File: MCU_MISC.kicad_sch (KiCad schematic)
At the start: 61 parts, among them J4 Conn_ARM_JTAG_SWD_20, J5 Conn_01x03, J6 Conn_01x03, J7 SMA, J8 SMA, SW1 焊盘, SW2 Push_Button, SW3 Push_Button, SW4 Push_Button, U10 TJA1044GTK/3Z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

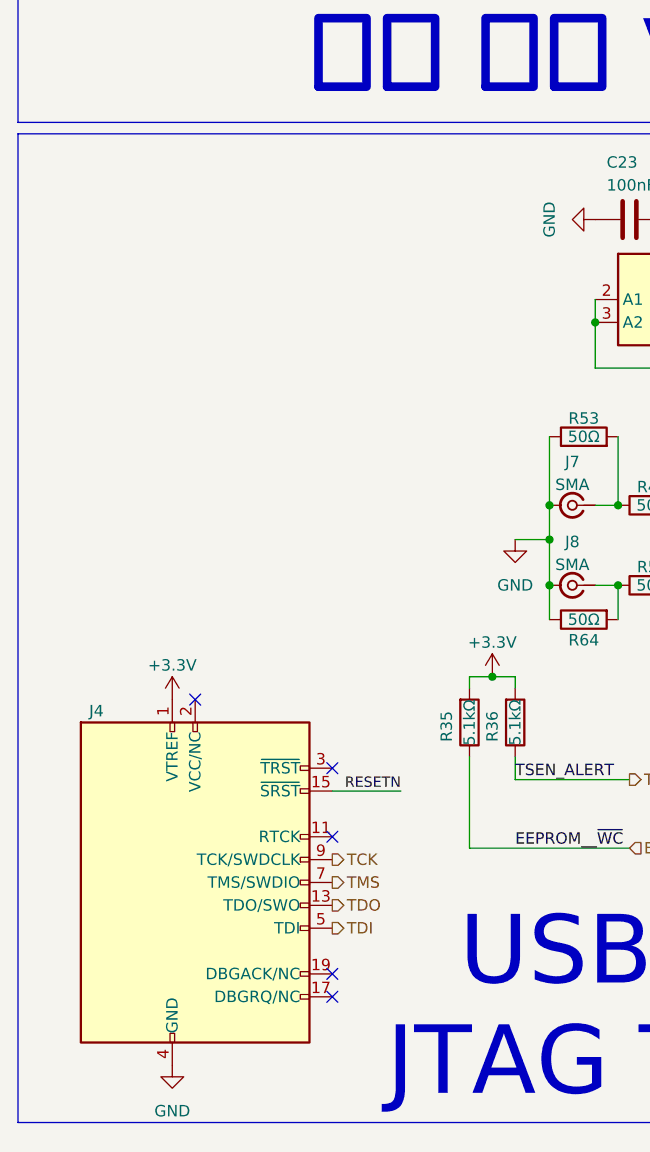
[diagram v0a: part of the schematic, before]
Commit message: 添加JTAG接口的ESD保护
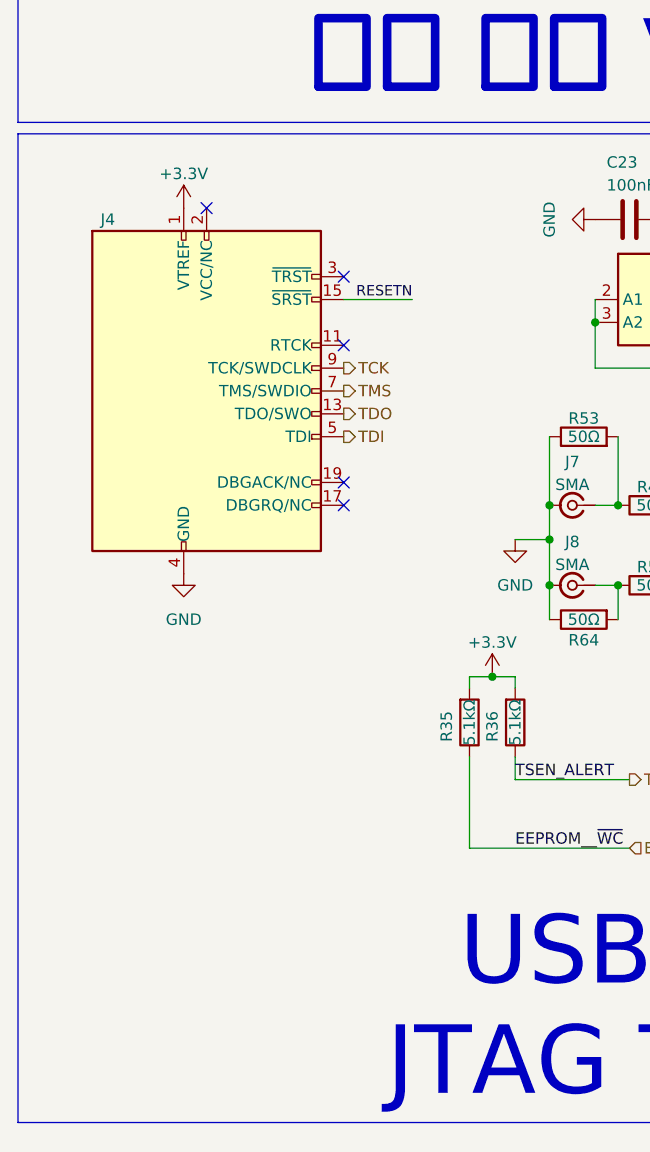
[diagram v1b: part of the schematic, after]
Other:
- moved on the sheet: J4
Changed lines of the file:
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@@
 	)
 	(no_connect
-		(at 46.99 181.61)
+		(at 48.26 127)
 	)
 	(no_connect
-		(at 31.75 151.13)
+		(at 33.02 96.52)
 	)
 	(no_connect
-		(at 46.99 158.75)
+		(at 48.26 104.14)
 	)
 	(no_connect
-		(at 46.99 184.15)
+		(at 48.26 129.54)
 	)
 	(no_connect
-		(at 46.99 166.37)
+		(at 48.26 111.76)
 	)
 	(wire
@@
 	(wire
 		(pts
-			(xy 46.99 161.29) (xy 54.61 161.29)
+			(xy 48.26 106.68) (xy 55.88 106.68)
 		)
 		(stroke
@@
 	)
 	(label "RESETN"
-		(at 54.61 161.29 180)
+		(at 55.88 106.68 180)
 		(effects
 			(font
@@
 	(hierarchical_label "TCK"
 		(shape output)
-		(at 46.99 168.91 0)
+		(at 48.26 114.3 0)
 		(effects
 			(font
@@
 	(hierarchical_label "TMS"
 		(shape output)
-		(at 46.99 171.45 0)
+		(at 48.26 116.84 0)
 		(effects
 			(font
@@
 	(hierarchical_label "TDO"
 		(shape output)
-		(at 46.99 173.99 0)
+		(at 48.26 119.38 0)
 		(effects
 			(font
@@
 	(hierarchical_label "TDI"
 		(shape output)
-		(at 46.99 176.53 0)
+		(at 48.26 121.92 0)
 		(effects
 			(font
@@
 		(lib_name "GND_1")
 		(lib_id "power:GND")
-		(at 29.21 191.77 0)
+		(at 30.48 137.16 0)
 		(unit 1)
 		(exclude_from_sim no)
@@
 		(fields_autoplaced yes)
 		(property "Reference" "#PWR0123"
-			(at 29.21 198.12 0)
+			(at 30.48 143.51 0)
 			(effects
 				(font
@@
 		)
 		(property "Value" "GND"
-			(at 29.21 196.85 0)
+			(at 30.48 142.24 0)
 			(effects
 				(font
@@
 		)
 		(property "Footprint" ""
-			(at 29.21 191.77 0)
+			(at 30.48 137.16 0)
 			(effects
 				(font
@@
 		)
 		(property "Datasheet" ""
-			(at 29.21 191.77 0)
+			(at 30.48 137.16 0)
 			(effects
 				(font
@@
 		)
 		(property "Description" "Power symbol creates a global label with name \"GND\" , ground"
-			(at 29.21 191.77 0)
+			(at 30.48 137.16 0)
 			(effects
 				(font
@@
 	(symbol
 		(lib_id "Connector:Conn_ARM_JTAG_SWD_20")
-		(at 31.75 171.45 0)
+		(at 33.02 116.84 0)
 		(unit 1)
 		(exclude_from_sim no)
@@
 		(dnp no)
 		(property "Reference" "J4"
-			(at 21.59 152.4 0)
+			(at 22.86 97.79 0)
 			(effects
 				(font
@@
 		)
 		(property "Value" "Conn_ARM_JTAG_SWD_20"
-			(at 17.78 172.7199 0)
+			(at 19.05 118.1099 0)
 			(effects
 				(font
@@
 		)
 		(property "Footprint" "Connector_IDC:IDC-Header_2x10_P2.54mm_Vertical"
-			(at 43.18 198.12 0)
+			(at 44.45 143.51 0)
 			(effects
 				(font
@@
 		)
 		(property "Datasheet" ""
-			(at 22.86 203.2 90)
+			(at 24.13 148.59 90)
 			(effects
 				(font
@@
 		)
 		(property "Description" ""
-			(at 31.75 171.45 0)
+			(at 33.02 116.84 0)
 			(effects
 				(font
@@
 	(symbol
 		(lib_id "power:+3.3V")
-		(at 29.21 151.13 0)
+		(at 30.48 96.52 0)
 		(unit 1)
 		(exclude_from_sim no)
@@
 		(dnp no)
 		(property "Reference" "#PWR098"
-			(at 29.21 154.94 0)
+			(at 30.48 100.33 0)
 			(effects
 				(font
@@
 		)
 		(property "Value" "+3.3V"
-			(at 29.21 147.32 0)
+			(at 30.48 92.71 0)
 			(effects
 				(font
@@
 		)
 		(property "Footprint" ""
-			(at 29.21 151.13 0)
+			(at 30.48 96.52 0)
 			(effects
 				(font
@@
 		)
 		(property "Datasheet" ""
-			(at 29.21 151.13 0)
+			(at 30.48 96.52 0)
 			(effects
 				(font
@@
 		)
 		(property "Description" ""
-			(at 29.21 151.13 0)
+			(at 30.48 96.52 0)
 			(effects
 				(font
